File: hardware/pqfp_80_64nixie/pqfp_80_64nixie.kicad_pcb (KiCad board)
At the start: 2 copper layers, 83.8 x 99.1 mm, 92 parts, among them J1 Conn_01x16, J2 Conn_01x16, J3 Conn_01x16, J4 Conn_01x16, J5 Conn_01x16, J6 NK01B, J7 Screw_Terminal_01x02, U1 PQFP-80

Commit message: Fixing NK01B pinout
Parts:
- removed G***: LOGO, IGG_64_breakout:woosh_text
- removed G***: LOGO, IGG_64_breakout:woosh_ralsei
- removed the REF** at (167.6, 119.4)
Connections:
- J6 pad 1: VIN -> GND
- J6 pad 2: GND -> Net-(J6-Pad2)
- J6 pad 3: PULSE -> RX
- J6 pad 4: Net-(J6-Pad4) -> /VOUT
- J6 pad 5: /VOUT -> Net-(J6-Pad5)
- J6 pad 6: RX -> PULSE
- J6 pad 7: Net-(J6-Pad7) -> GND
- J6 pad 8: GND -> VIN
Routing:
- net GND: track 93.2 -> 53.0 mm
- net VIN: track 90.9 -> 76.6 mm
- net PULSE: track 18.0 -> 12.2 mm
- net RX: track 25.4 -> 31.1 mm
- net /VOUT: track 27.7 -> 28.8 mm

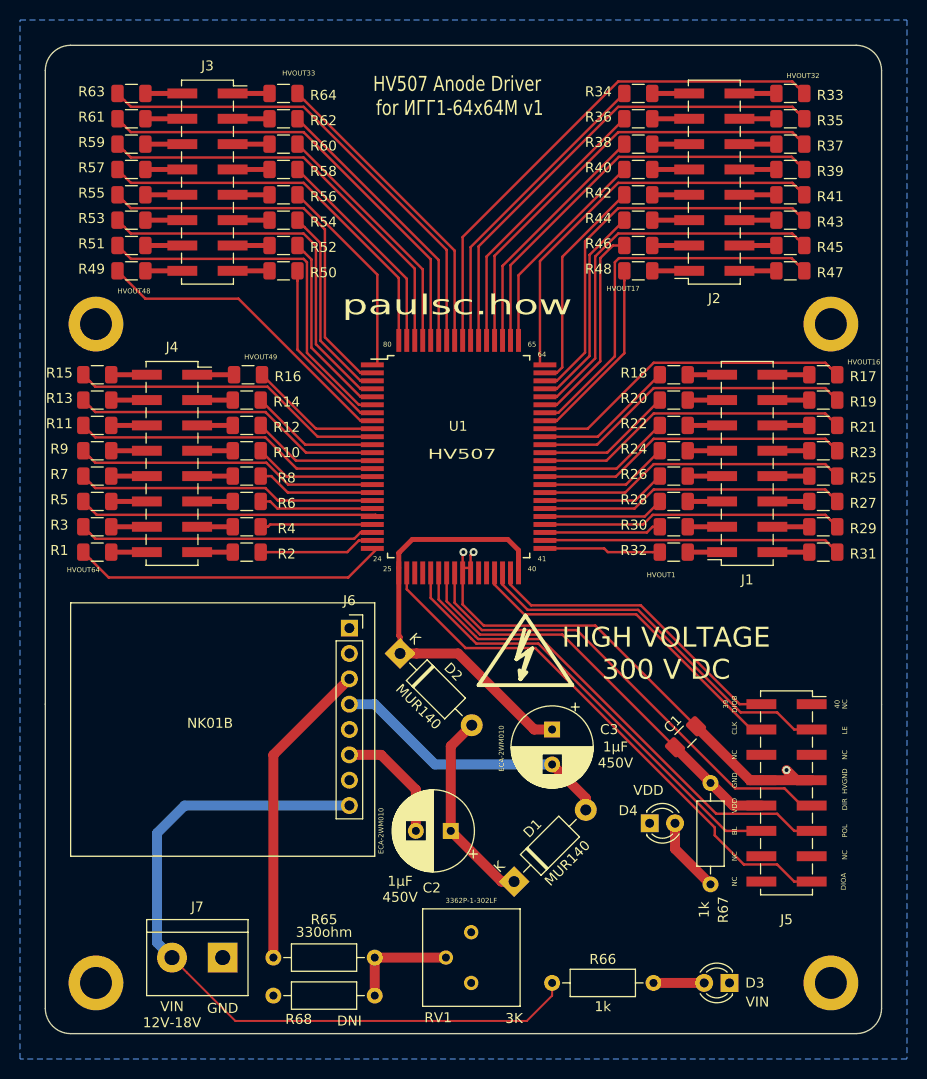
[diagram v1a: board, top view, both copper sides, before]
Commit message: New header footprint
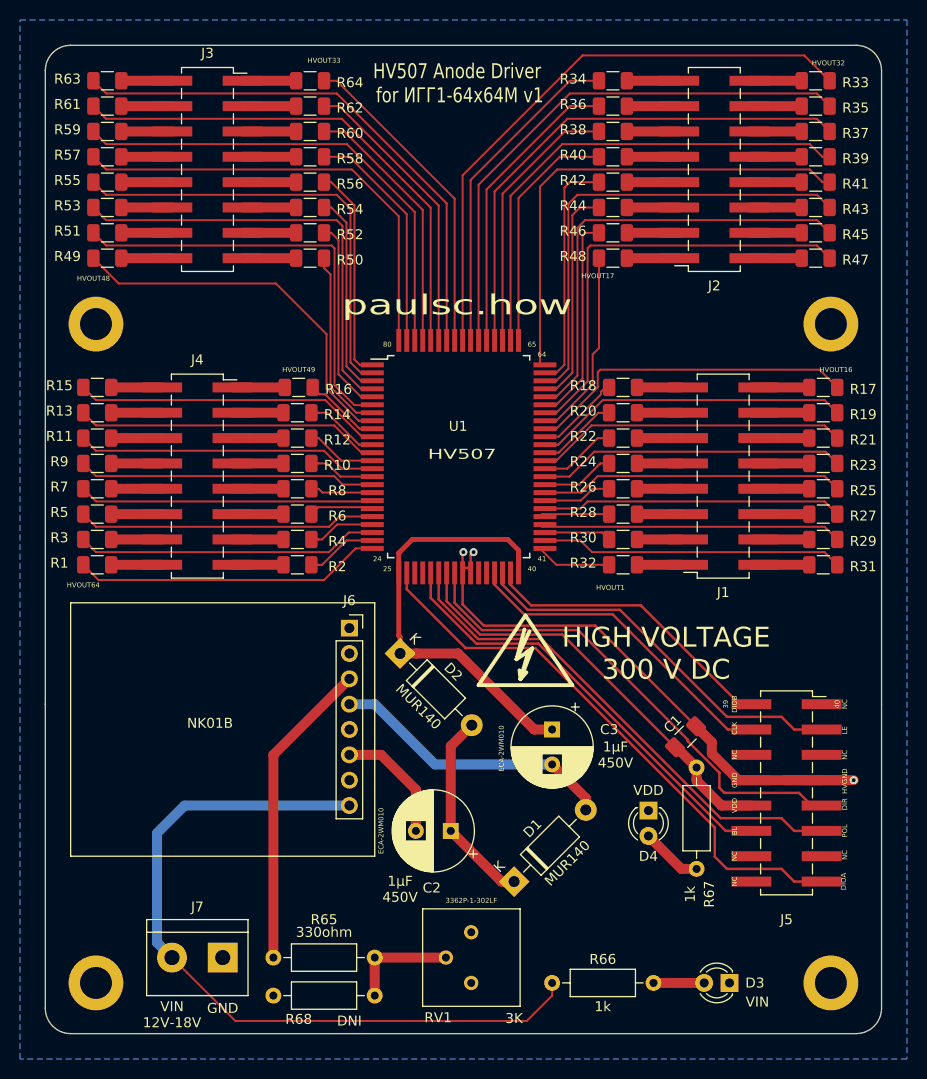
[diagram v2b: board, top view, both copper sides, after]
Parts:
- J1, J2, J3, J4, J5: footprint Connector_PinSocket_2.54mm:PinSocket_2x08_P2.54mm_Vertical_SMD -> IGG_64_breakout:PinSocket_2x08_P2.54mm_Vertical_SMD_L
- moved R10 5.24 mm to (134.5, 74.9)
- moved R2 5.24 mm to (134.5, 85.1)
- moved R6 5.24 mm to (134.5, 80.0)
- moved R12 5.24 mm to (134.5, 72.4)
- moved R14 5.24 mm to (134.5, 69.8)
- moved R16 5.24 mm to (134.6, 67.3)
- moved R4 5.24 mm to (134.5, 82.5)
- moved R8 5.24 mm to (134.5, 77.5)
- moved R24 5.24 mm to (167.1, 74.9)
- moved R28 5.24 mm to (167.1, 80.0)
- moved R32 5.24 mm to (167.1, 85.1)
- moved R18 5.24 mm to (167.1, 67.3)
- moved R20 5.24 mm to (167.1, 69.8)
- moved R22 5.24 mm to (167.1, 72.4)
- moved R26 5.24 mm to (167.1, 77.5)
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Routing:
- net HVOUT32: track 52.1 -> 59.9 mm
- net /HVOUT24: track 40.6 -> 48.1 mm
- net 66: track 42.5 -> 49.6 mm
- net 68: track 45.7 -> 52.6 mm
- net 70: track 48.9 -> 55.6 mm
- net HVOUT40: track 39.5 -> 46.0 mm
- net Net-(R43-Pad2): track 40.7 -> 47.0 mm
- net HVOUT38: track 42.7 -> 48.9 mm
- net HVOUT48: track 32.3 -> 38.4 mm
- net 76: track 45.9 -> 51.8 mm
- net Net-(R45-Pad2): track 39.7 -> 45.6 mm
- net HVOUT46: track 38.0 -> 43.7 mm
- net HVOUT42: track 39.8 -> 45.4 mm
- net HVOUT44: track 38.8 -> 44.5 mm
- net /HVOUT49: track 13.8 -> 8.19 mm
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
